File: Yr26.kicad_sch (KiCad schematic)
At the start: 0 parts

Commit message: BiProp26 GFS PNID
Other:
- added sheet GFS (Concept) (GFSYr26.kicad_sch)
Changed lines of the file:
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@@
 	(generator_version "9.0")
 	(paper "A4")
+	(sheet
+		(at 16.51 16.51)
+		(size 59.69 49.53)
+		(exclude_from_sim no)
+		(in_bom yes)
+		(on_board yes)
+		(dnp no)
+		(fields_autoplaced yes)
+		(stroke
+			(width 0.1524)
+			(type solid)
+		)
+		(fill
+			(color 0 0 0 0.0000)
+		)
+		(property "Sheetname" "GFS (Concept)"
+			(at 16.51 15.7984 0)
+			(effects
+				(font
+					(size 1.27 1.27)
+				)
+				(justify left bottom)
+			)
+		)
+		(property "Sheetfile" "GFSYr26.kicad_sch"
+			(at 16.51 66.6246 0)
+			(effects
+				(font
+					(size 1.27 1.27)
+				)
+				(justify left top)
+			)
+		)
+		(instances
+			(project "P_IDs"
+				(path "/045f1f05-3134-4b6d-91b6-463031104f1e/a0b6300e-76e9-4a18-afd6-e2d656b0d8f9"
+					(page "19")
+				)
+			)
+		)
+	)
 )

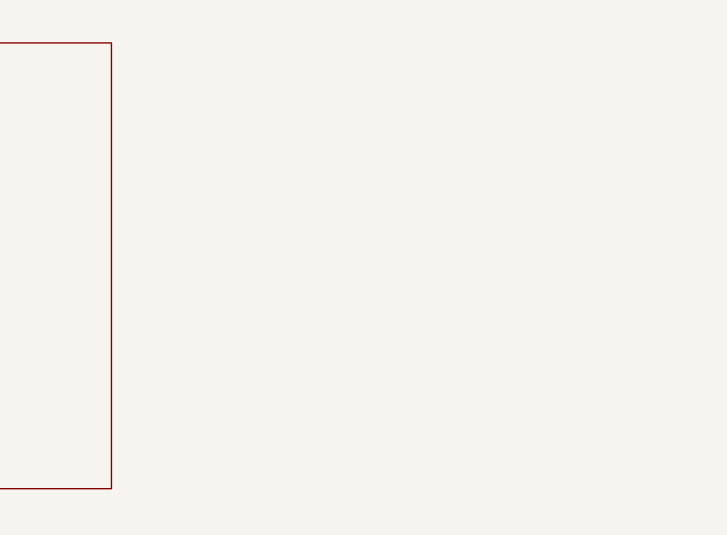
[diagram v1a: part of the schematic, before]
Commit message: Feed System Work
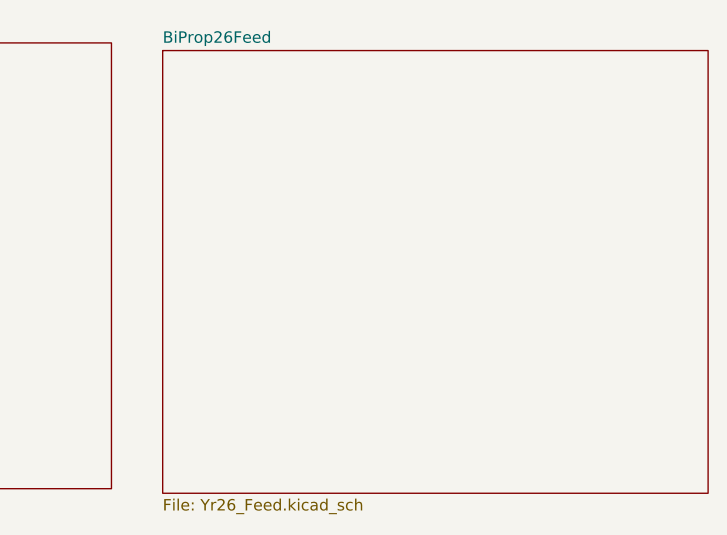
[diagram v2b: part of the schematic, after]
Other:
- added sheet BiProp26Feed (Yr26_Feed.kicad_sch)
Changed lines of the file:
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@@
+		)
+	)
+	(sheet
+		(at 81.892 17.3601)
+		(size 60.602 49.1879)
+		(exclude_from_sim no)
+		(in_bom yes)
+		(on_board yes)
+		(dnp no)
+		(fields_autoplaced yes)
+		(stroke
+			(width 0.1524)
+			(type solid)
+		)
+		(fill
+			(color 0 0 0 0.0000)
+		)
+		(property "Sheetname" "BiProp26Feed"
+			(at 81.892 16.6485 0)
+			(effects
+				(font
+					(size 1.27 1.27)
+				)
+				(justify left bottom)
+			)
+		)
+		(property "Sheetfile" "Yr26_Feed.kicad_sch"
+			(at 81.892 67.1326 0)
+			(effects
+				(font
+					(size 1.27 1.27)
+				)
+				(justify left top)
+			)
+		)
+		(instances
+			(project "P_IDs"
+				(path "/045f1f05-3134-4b6d-91b6-463031104f1e/a0b6300e-76e9-4a18-afd6-e2d656b0d8f9"
+					(page "20")
+				)
+			)
 		)
 	)

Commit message: feedfeed
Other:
- added sheet Silwood Project (J0.kicad_sch)
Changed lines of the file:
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@@
+		)
+	)
+	(sheet
+		(at 25.4 82.55)
+		(size 73.66 50.8)
+		(exclude_from_sim no)
+		(in_bom yes)
+		(on_board yes)
+		(dnp no)
+		(fields_autoplaced yes)
+		(stroke
+			(width 0.1524)
+			(type solid)
+		)
+		(fill
+			(color 0 0 0 0.0000)
+		)
+		(property "Sheetname" "Silwood Project"
+			(at 25.4 81.8384 0)
+			(effects
+				(font
+					(size 1.27 1.27)
+				)
+				(justify left bottom)
+			)
+		)
+		(property "Sheetfile" "J0.kicad_sch"
+			(at 25.4 133.9346 0)
+			(effects
+				(font
+					(size 1.27 1.27)
+				)
+				(justify left top)
+			)
+		)
+		(instances
+			(project "P_IDs"
+				(path "/045f1f05-3134-4b6d-91b6-463031104f1e/a0b6300e-76e9-4a18-afd6-e2d656b0d8f9"
+					(page "21")
+				)
+			)
 		)
 	)

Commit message: andrei it support
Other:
- removed sheet BiProp26Feed
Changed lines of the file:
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@@
 	)
 	(sheet
-		(at 81.892 17.3601)
-		(size 60.602 49.1879)
+		(at 16.51 74.295)
+		(size 59.055 38.1)
 		(exclude_from_sim no)
 		(in_bom yes)
@@
 			(color 0 0 0 0.0000)
 		)
-		(property "Sheetname" "BiProp26Feed"
-			(at 81.892 16.6485 0)
+		(property "Sheetname" "Silwood Project"
+			(at 16.51 73.5834 0)
 			(effects
 				(font
@@
 			)
 		)
-		(property "Sheetfile" "Yr26_Feed.kicad_sch"
-			(at 81.892 67.1326 0)
+		(property "Sheetfile" "J0.kicad_sch"
+			(at 16.51 112.9796 0)
 			(effects
 				(font
@@
 				)
 			)
-		)
-	)
-	(sheet
-		(at 25.4 82.55)
-		(size 73.66 50.8)
-		(exclude_from_sim no)
-		(in_bom yes)
-		(on_board yes)
-		(dnp no)
-		(fields_autoplaced yes)
-		(stroke
-			(width 0.1524)
-			(type solid)
-		)
-		(fill
-			(color 0 0 0 0.0000)
-		)
-		(property "Sheetname" "Silwood Project"
-			(at 25.4 81.8384 0)
-			(effects
-				(font
-					(size 1.27 1.27)
-				)
-				(justify left bottom)
-			)
-		)
-		(property "Sheetfile" "J0.kicad_sch"
-			(at 25.4 133.9346 0)
-			(effects
-				(font
-					(size 1.27 1.27)
-				)
-				(justify left top)
-			)
-		)
-		(instances
-			(project "P_IDs"
-				(path "/045f1f05-3134-4b6d-91b6-463031104f1e/a0b6300e-76e9-4a18-afd6-e2d656b0d8f9"
-					(page "21")
-				)
-			)

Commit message: Feediddy
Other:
- removed sheet Silwood Project
- added sheet BiProp26Feed (Yr26_Feed.kicad_sch)
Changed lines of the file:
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@@
 	)
 	(sheet
-		(at 16.51 74.295)
-		(size 59.055 38.1)
+		(at 81.892 17.3601)
+		(size 60.602 49.1879)
 		(exclude_from_sim no)
 		(in_bom yes)
@@
 			(color 0 0 0 0.0000)
 		)
-		(property "Sheetname" "Silwood Project"
-			(at 16.51 73.5834 0)
+		(property "Sheetname" "BiProp26Feed"
+			(at 81.892 16.6485 0)
 			(effects
 				(font
@@
 			)
 		)
-		(property "Sheetfile" "J0.kicad_sch"
-			(at 16.51 112.9796 0)
+		(property "Sheetfile" "Yr26_Feed.kicad_sch"
+			(at 81.892 67.1326 0)
 			(effects
 				(font
